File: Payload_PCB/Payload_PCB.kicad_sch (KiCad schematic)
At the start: 30 parts, among them J1 Conn_01x03, J2 Conn_01x03, J3 Conn_01x03, J4 Conn_01x03, J5 43650-0400, Q1 PMOS, Q12 PMOS, Q2 PMOS, Q3 PMOS, U10 TSR_1-2450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

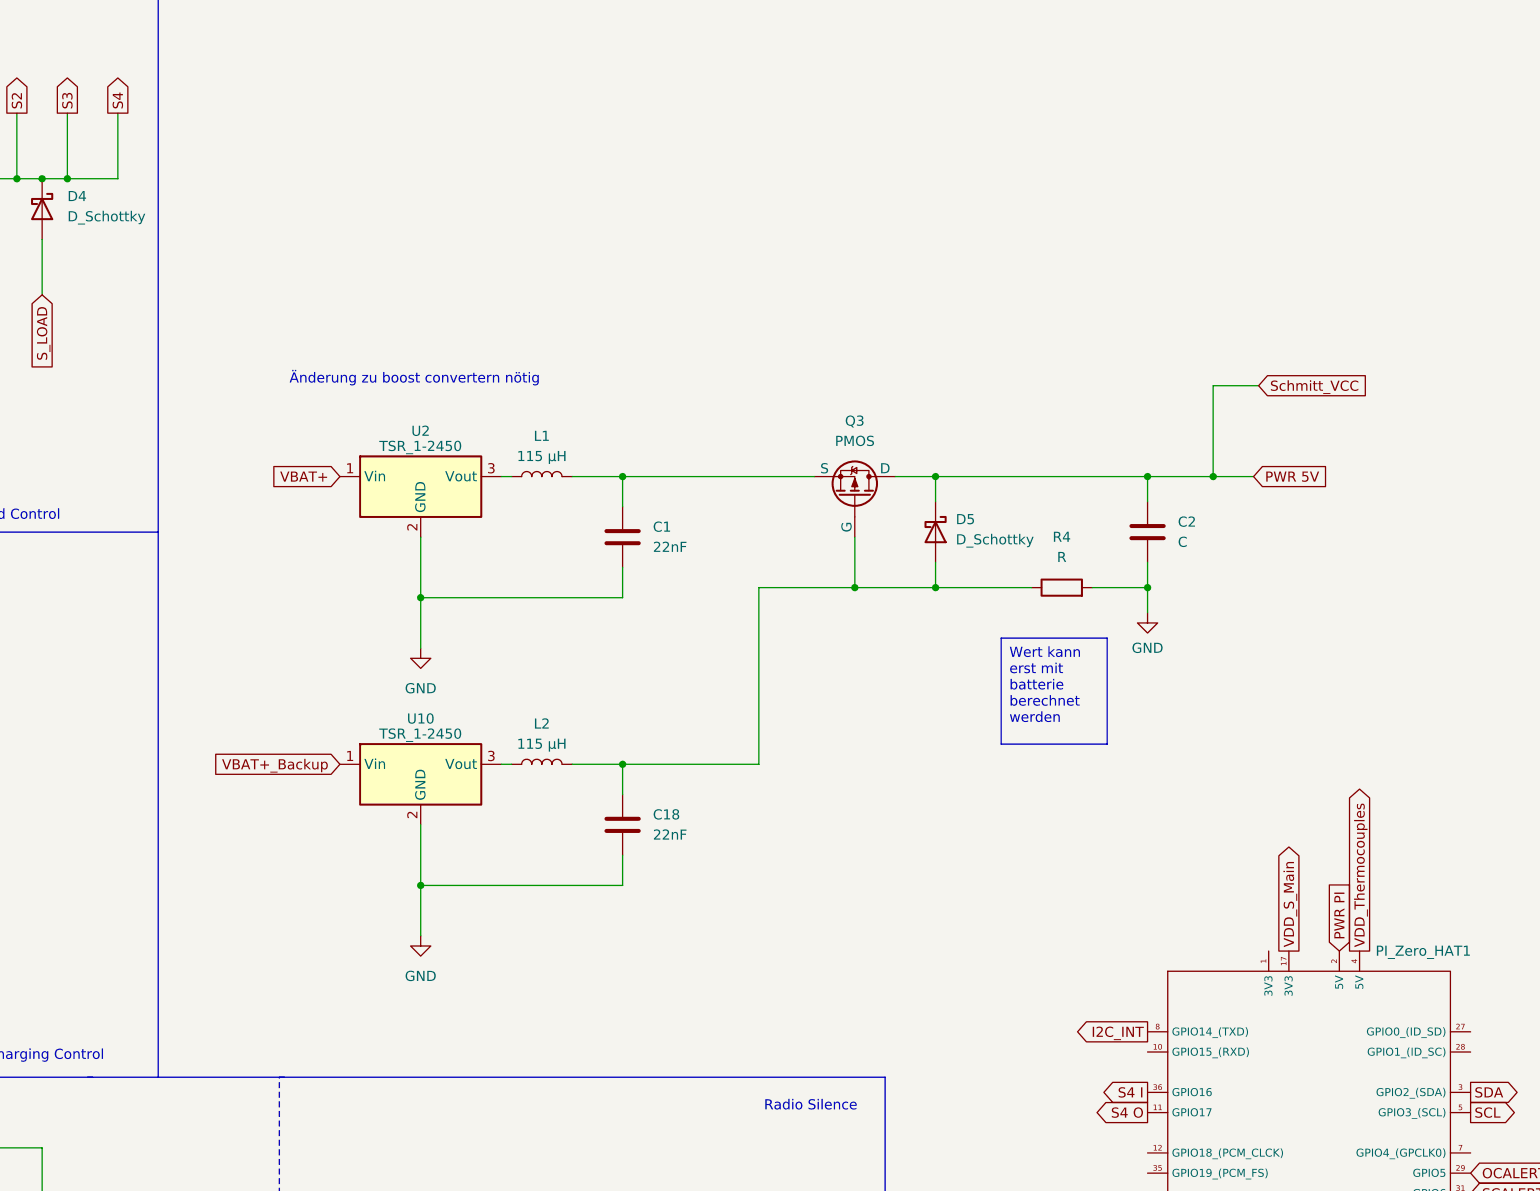
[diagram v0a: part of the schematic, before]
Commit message: Changed buck converter to boost converter
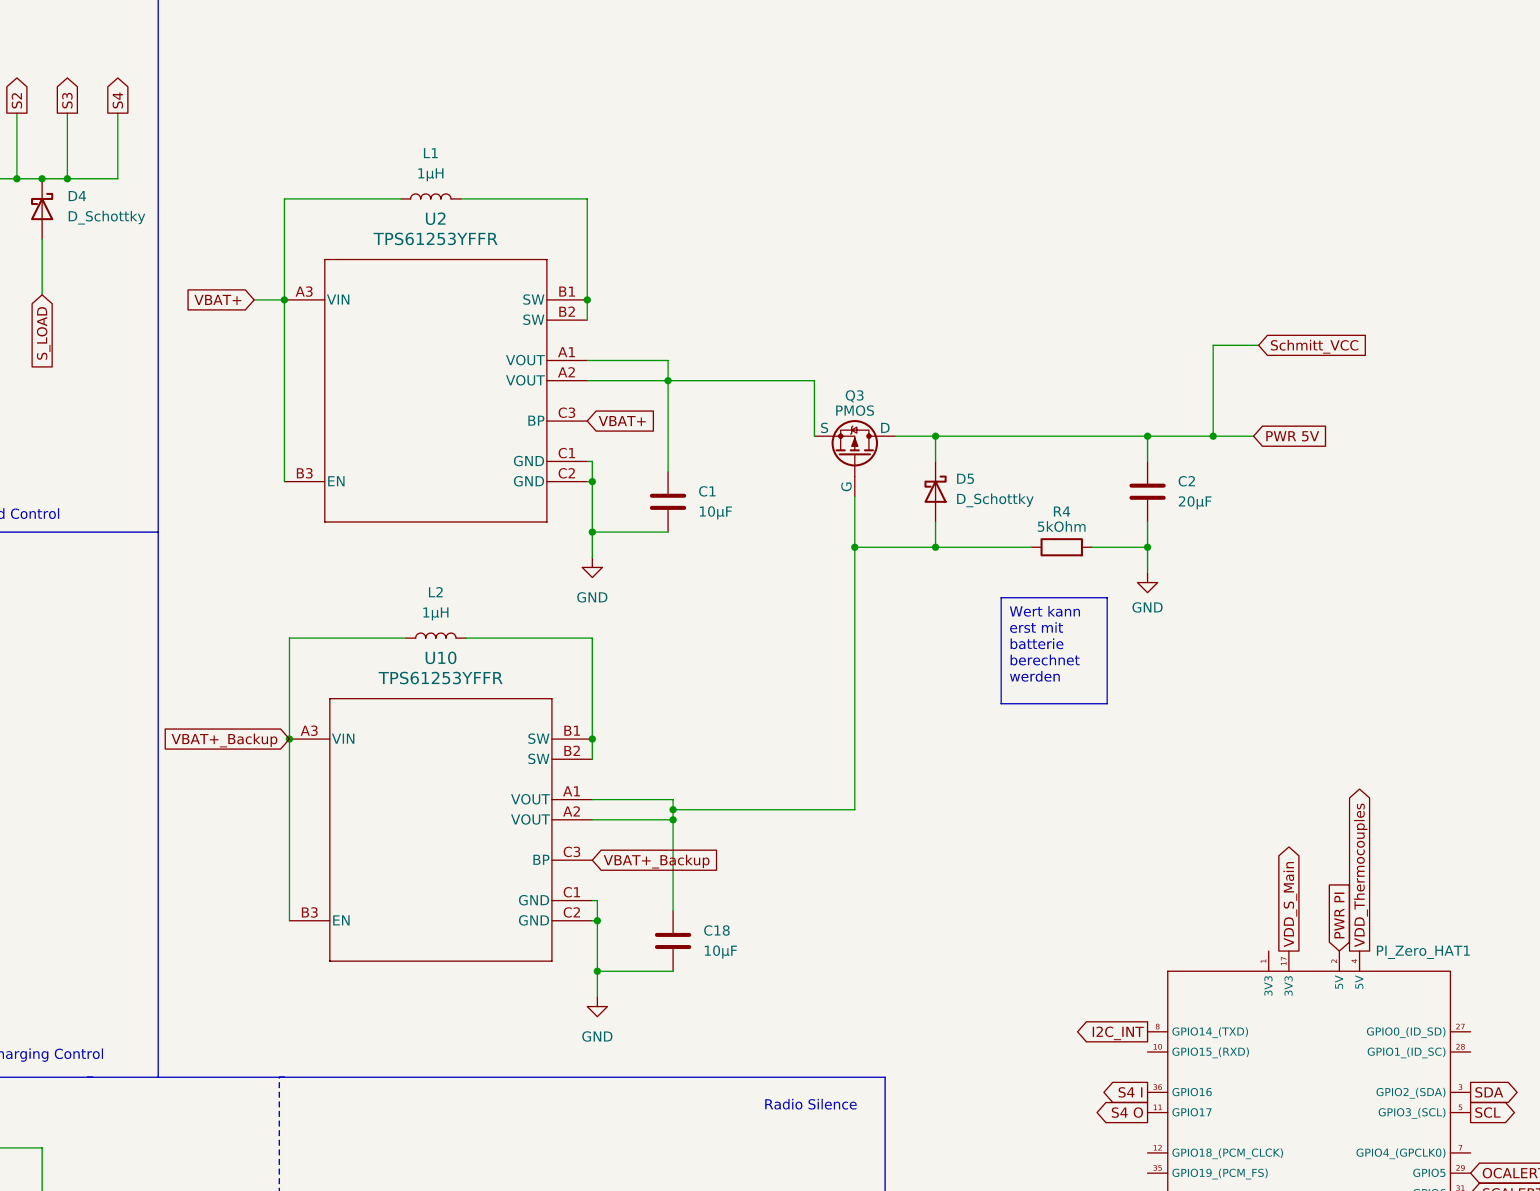
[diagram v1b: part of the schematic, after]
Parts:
- removed U10, U2: TSR_1-2450, Converter_DCDC:Converter_DCDC_TRACO_TSR-1_THT, symbol Regulator_Switching:TSR_1-2450
- added U10, U2: TPS61253YFFR, YFF0009ACAG, symbol 2024-02-22_21-04-40:TPS61253YFFR
- C1, C18: value 22nF -> 10µF
- C2: value C -> 20µF
- L1, L2: value 115 µH -> 1µH
- R4: value R -> 5kOhm
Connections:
- net GND: now also U10.C1 (GND), U10.C2 (GND), U2.C1 (GND), U2.C2 (GND)
- net VBAT+: now also L1.1, U2.A3 (VIN), U2.B3 (EN), U2.C3 (BP)
- net VBAT+_Backup: now also L2.1, U10.A3 (VIN), U10.B3 (EN), U10.C3 (BP)
- net at C18.1, D5.2 (A), Q3.2 (G)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: now also U10.A1 (VOUT), U10.A2 (VOUT); no longer L2.2
- net at C1.1, Q3.3 (S): now also U2.A1 (VOUT), U2.A2 (VOUT); no longer L1.2
- new net: L1.2, U2.B1 (SW), U2.B2 (SW)
- new net: L2.2, U10.B1 (SW), U10.B2 (SW)
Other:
- note removed: "Änderung zu boost convertern nötig"
- moved on the sheet: C1, C2, D5, L1, Q3, R4

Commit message: Add BMS Chip and Radio Silence
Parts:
- removed C21: 0.1uF, symbol Device:C
- removed Q1, Q12, Q2: PMOS, symbol Simulation_SPICE:PMOS
- removed R3: 10kOhm, symbol Device:R
- removed R47: 10 Ohm, symbol Device:R
- added D26, D27: D_Schottky, symbol Device:D_Schottky
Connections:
- net PWR 5V: no longer D1.1 (K), U1.5 (VCC), cutoff_plug1.1
- net Light: now reaches PI_Zero_HAT1.32 (GPIO12_(PWM0))
- net Heater_CTRL: now reaches PI_Zero_HAT1.33 (GPIO13_(PWM1))
- net Bat_Check: no longer names the net of J5.3
- net Bat_Check: now also D26.1 (K), D27.1 (K)
- new net Bat_CheckC: D26.2 (A)
- new net Bat_CheckD: D27.2 (A)
- new net Schmitt_VCC: D1.1 (K), U1.5 (VCC), cutoff_plug1.1
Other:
- sheet BMS_MCP73834 renamed Charge_MCP73834_1
- sheet BMS_MCP73835 renamed Charge_MCP73834_2
- note added: "Boost to 5V and power select between Main and Backup"
- note added: "Radio Silence Main Part"
- moved on the sheet: C1, C18, C2, D1, D2, D3, D5, J5, L1, L2, PI_Zero_HAT1, Q3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

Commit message: Changed some radio silence
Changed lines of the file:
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@@
+    (stroke (width 0) (type default))
+  )
+  (wire (pts (xy 86.36 220.98) (xy 86.36 226.06))
     (stroke (width 0) (type default))
   )
@@
   )
   (wire (pts (xy 94.615 87.63) (xy 97.79 87.63))
+    (stroke (width 0) (type default))
+  )
+  (wire (pts (xy 86.36 226.06) (xy 88.9 226.06))
     (stroke (width 0) (type default))
   )
@@
       (effects (font (size 1.27 1.27)) (justify left) hide)
     )
+  )
+  (global_label "Short{slash}Discharge" (shape output) (at 88.9 226.06 0) (fields_autoplaced)
+    (effects (font (size 1.27 1.27)) (justify left))
+    (property "Intersheetrefs" "${INTERSHEET_REFS}" (at 107.5484 226.06 0)
+      (effects (font (size 1.27 1.27)) (justify left) hide)
+    )

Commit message: Added heating pad, adjustment of page sizes
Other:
- added sheet Heating Pad Control 1 (heating_pad.kicad_sch)
- added sheet Heating Pad Control 2 (heating_pad.kicad_sch)
- added sheet Heating Pad Control 3 (heating_pad.kicad_sch)
- note added: "Heating Pad control"
- note removed: "TODO: Maybe only one VDD and distribute among sensors?"
- moved on the sheet: PI_Zero_HAT1

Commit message: Added some actual parts
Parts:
- removed D1, D2, D26, D27, D3, D4, D5: D_Schottky, symbol Device:D_Schottky
- added D1, D2, D3: RB511VM-30TE-17, RB511VM30TE17, symbol RB511VM-30TE-17:RB511VM-30TE-17
- added D5: B5819WS-TP, SOD2512X115N, symbol B5819WS-TP:B5819WS-TP
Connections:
- net Bat_CheckC: now also J5.3
- net Light: now also PI_Zero_HAT1.1 (3V3); no longer PI_Zero_HAT1.32 (GPIO12_(PWM0))
- net PWR 5V: now also D5.1 (K)
- net RS_Gate: now also D2.1 (K), D3.1 (K)
- net Schmitt_Out: now also D2.2 (A)
- net Schmitt_VCC: now also D1.1 (K)
- net VDD: now also D1.2 (A)
- net at C18.1, Q3.2 (G), R4.1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: now also D5.2 (A)
- net at cutoff_plug1.2: now also D3.2 (A)
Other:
- company: (none) -> SpaceTeam Aachen
- title: (none) -> Payload Root Page

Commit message: Change to actual real parts
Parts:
- removed U1: ~, Package_TO_SOT_SMD:SOT-553, symbol 74xGxx:SN74LVC1G14DRL
- added IC6: BU4S584G2-TL, SOT95P280X125-5N, symbol BU4S584G2-TL:BU4S584G2-TL
- added LED_Conn1: Conn_01x03_Pin, symbol Connector:Conn_01x03_Pin
- added MicroSD_Conn1: Conn_01x06_Pin, symbol Connector:Conn_01x06_Pin
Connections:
- net Light is gone; now on net VDD_Thermocouples: PI_Zero_HAT1.1 (3V3)
- net GND: now also IC6.3 (VSS), LED_Conn1.1 (Pin_1), MicroSD_Conn1.6 (Pin_6)
- net Schmitt_Out: now also IC6.4 (Y)
- net Schmitt_VCC: now also IC6.5 (VDD)
- net VDD_Thermocouples: no longer PI_Zero_HAT1.4 (5V)
- net at R1.2, R2.1: now also IC6.2 (A)
- net MOSI_SD: now reaches PI_Zero_HAT1.19 (GPIO10_(MOSI))
- net MOSI_SD: now also MicroSD_Conn1.3 (Pin_3)
- net MISO_SD: now reaches PI_Zero_HAT1.21 (GPIO9_(MISO))
- net MISO_SD: now also MicroSD_Conn1.5 (Pin_5)
- net CLK_SD: now reaches PI_Zero_HAT1.23 (GPIO11_(SCLK))
- net CLK_SD: now also MicroSD_Conn1.4 (Pin_4)
- net CE_SD: now reaches PI_Zero_HAT1.24 (GPIO8_(CE0))
- net CE_SD: now also MicroSD_Conn1.2 (Pin_2)
- net 3V3_SD: now reaches PI_Zero_HAT1.26 (GPIO7_(CE1))
- net 3V3_SD: now also MicroSD_Conn1.1 (Pin_1)
- net LED_CTRL: now reaches PI_Zero_HAT1.32 (GPIO12_(PWM0))
- net LED_CTRL: now also LED_Conn1.3 (Pin_3)
- new net LED_PWR: LED_Conn1.2 (Pin_2), PI_Zero_HAT1.4 (5V)
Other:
- note added: "3.3V"
- note added: "Black GND"
- note added: "Blue DI"
- note added: "CLK"
- note added: "CS"
- note added: "Connector to external micro SD card"
- note added: "GND"
- note added: "LED Ring Connector"
- note added: "MISO"
- note added: "MOSI"
- note added: "Red 5V"
- note added: "Schmitt Inverter"
- note added: "Sensors"
- moved on the sheet: J5

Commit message: some new parts
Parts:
- removed D3: RB511VM-30TE-17, RB511VM30TE17, symbol RB511VM-30TE-17:RB511VM-30TE-17
- removed IC6: BU4S584G2-TL, SOT95P280X125-5N, symbol BU4S584G2-TL:BU4S584G2-TL
- removed J1, J2, J3, J4: Conn_01x03, symbol Connector_Generic:Conn_01x03
- removed LED_Conn1: Conn_01x03_Pin, symbol Connector:Conn_01x03_Pin
- added D4: RB511VM-30TE-17, footprints:RB511VM30TE17, symbol RB511VM-30TE-17:RB511VM-30TE-17
- added IC1: BU4S584G2-TL, footprints:SOT95P280X125-5N, symbol BU4S584G2-TL:BU4S584G2-TL
- added J1, J2, J3, J4, LED_Conn1: 43650-0315, footprints:43650-03YY_151617, symbol 43650-0315:43650-0315
- D1, D2: footprint RB511VM30TE17 -> footprints:RB511VM30TE17
- D5: footprint SOD2512X115N -> footprints:SOD2512X115N
- J5: footprint 43650-0400:MOLEX_43650-0400 -> footprints:MOLEX_43650-0400
- U10, U2: footprint YFF0009ACAG -> footprints:YFF0009ACAG
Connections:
- net GND: now also IC1.3 (VSS), J1.1, J2.1, J3.1, J4.1, LED_Conn1.3
- net LED_CTRL: now also PI_Zero_HAT1.12 (GPIO18_(PCM_CLCK)), LED_Conn1.1; no longer PI_Zero_HAT1.32 (GPIO12_(PWM0))
- net LED_PWR: now also LED_Conn1.2
- net RS_Gate: now also D1.1 (K)
- net Schmitt_Out: now also D1.2 (A), IC1.4 (Y); no longer D2.2 (A)
- net Schmitt_VCC: now also D4.1 (K), IC1.5 (VDD); no longer D1.1 (K)
- net Solenoid Control 1/s_blue: now also J1.3
- net Solenoid Control 1/s_white: now also J1.2
- net Solenoid Control 2/s_blue: now also J2.3
- net Solenoid Control 2/s_white: now also J2.2
- net Solenoid Control 3/s_blue: now also J3.3
- net Solenoid Control 3/s_white: now also J3.2
- net Solenoid Control 4/s_blue: now also J4.3
- net Solenoid Control 4/s_white: now also J4.2
- net VDD: now also D4.2 (A); no longer D1.2 (A)
- net at R1.2, R2.1: now also IC1.2 (A)
- net at cutoff_plug1.2: now also D2.2 (A)
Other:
- note added: "B DI"
- note added: "GND (R)"
- note added: "IN (B)"
- note added: "OUT (W)"
- note added: "R 5V"
- note added: "S GND"
- note removed: "Black GND"
- note removed: "Blue DI"
- note removed: "Red 5V"
